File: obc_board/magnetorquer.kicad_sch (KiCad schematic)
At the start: 44 parts

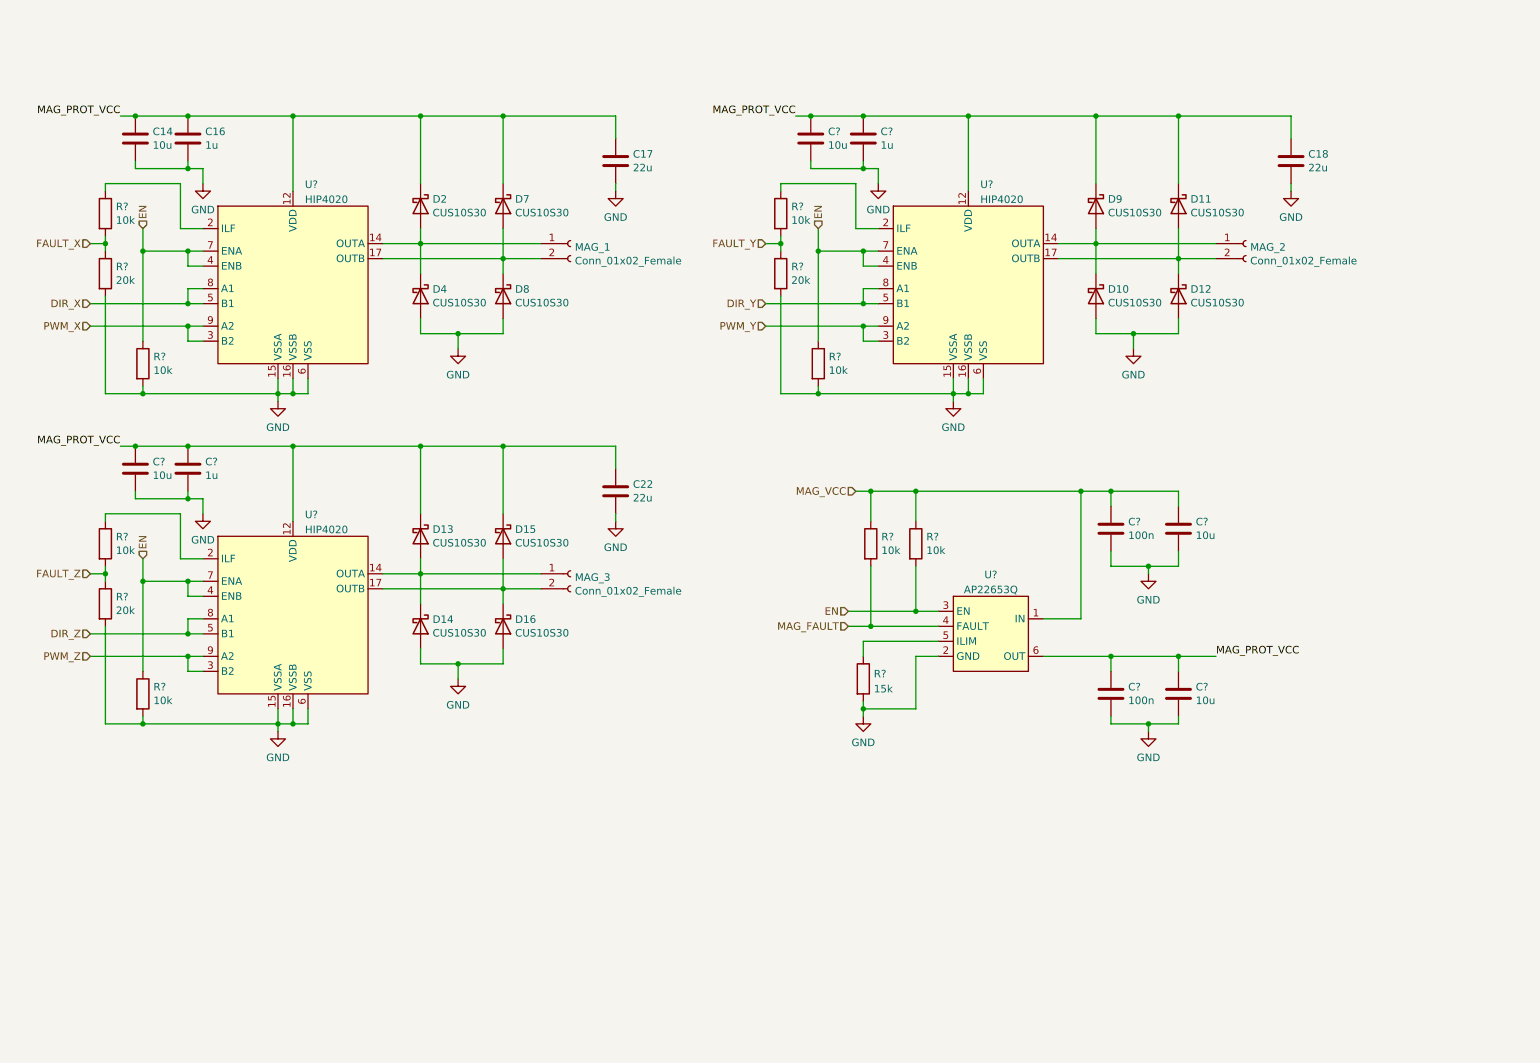
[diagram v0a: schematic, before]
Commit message: changed magnetorquer driver IC and changed power switch IC
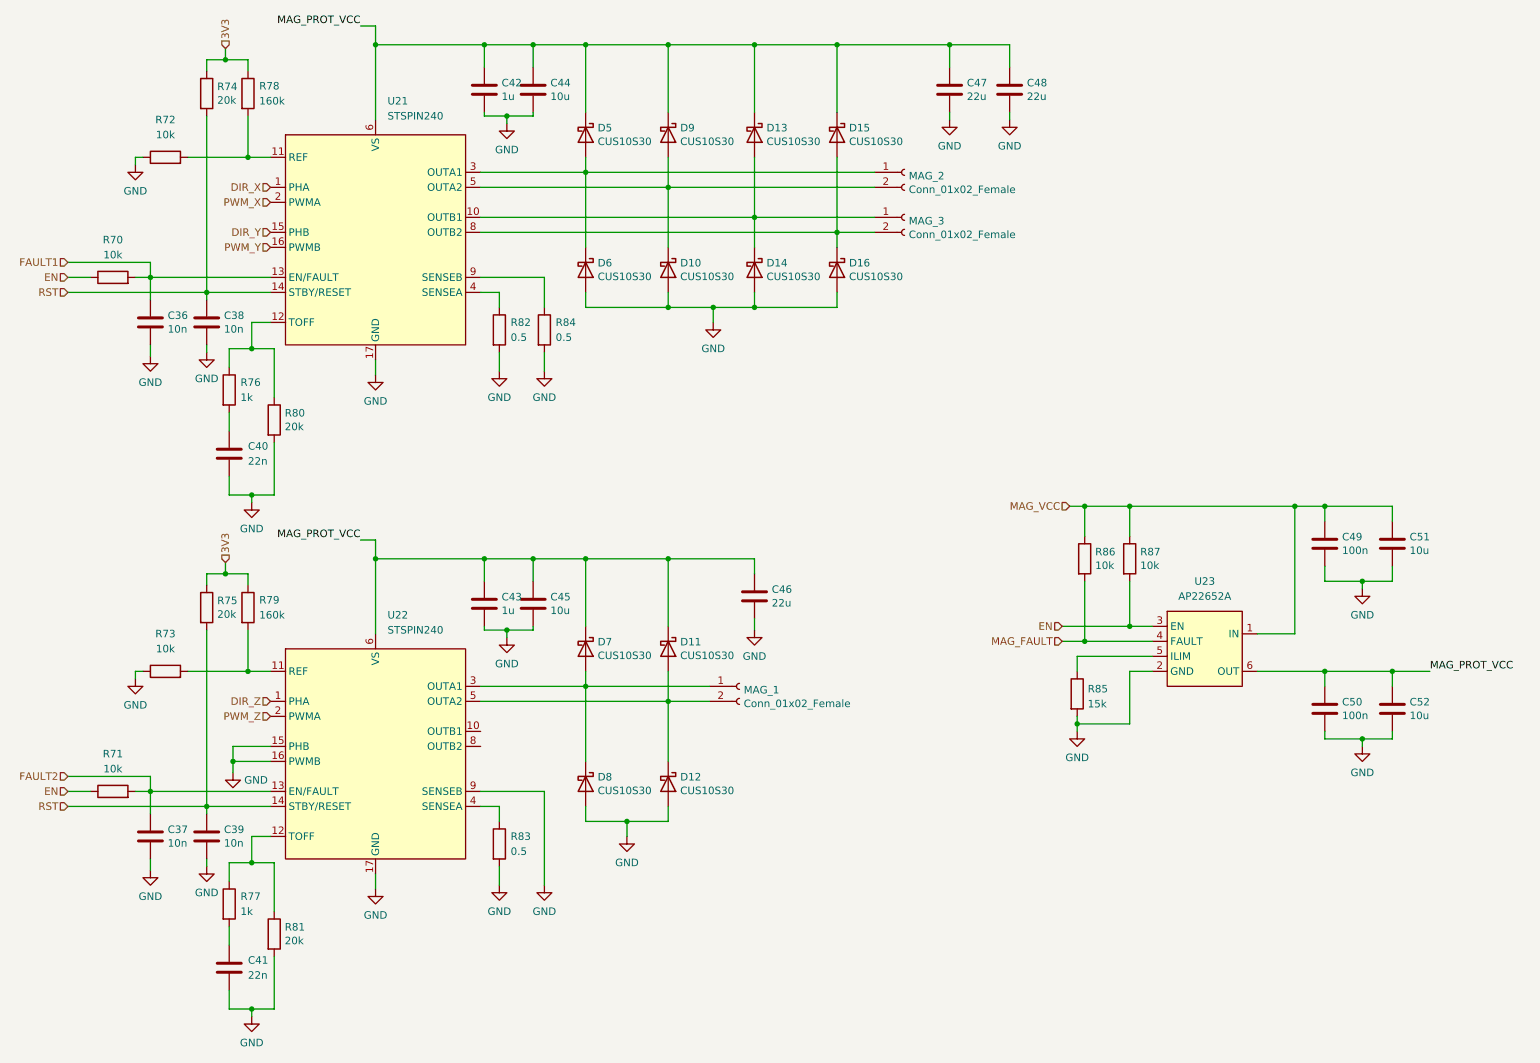
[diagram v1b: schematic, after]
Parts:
- removed C14, C? (x2): 10u, Capacitor_SMD:C_1206_3216Metric, symbol Device:C
- removed C16, C? (x2): 1u, Capacitor_SMD:C_0603_1608Metric, symbol Device:C
- removed R? (x6): 10k, Resistor_SMD:R_0402_1005Metric, symbol Device:R
- removed R? (x3): 20k, Resistor_SMD:R_0603_1608Metric, symbol Device:R
- removed U? (x3): HIP4020, symbol cubesat_obc_lib:HIP4020
- removed U?: AP22653Q, symbol cubesat_obc_lib:AP22653Q
- added C36, C37, C38, C39: 10n, Capacitor_SMD:C_0805_2012Metric, symbol Device:C
- added C40, C41: 22n, symbol Device:C
- added C42, C43: 1u, Capacitor_SMD:C_0603_1608Metric, symbol Device:C
- added C44, C45: 10u, Capacitor_SMD:C_1206_3216Metric, symbol Device:C
- added R70, R71, R72, R73: 10k, Resistor_SMD:R_0402_1005Metric, symbol Device:R
- added R74, R75, R80, R81: 20k, Resistor_SMD:R_0603_1608Metric, symbol Device:R
- added R76, R77: 1k, Resistor_SMD:R_0402_1005Metric, symbol Device:R
- added R78, R79: 160k, symbol Device:R
- added R82, R83, R84: 0.5, symbol Device:R
- added U21, U22: STSPIN240, symbol cubesat_obc_lib:STSPIN240
- added U23: AP22652A, symbol cubesat_obc_lib:AP22652A
- gave numbers to parts that had none: 7
- renumbered C22 to C46, C18 to C47, C17 to C48, D8 to D10, D15 to D11, D16 to D12, D9 to D13, D10 to D14, D11 to D15, D12 to D16, D2 to D5, D4 to D6, D13 to D7, D14 to D8, D7 to D9, MAG_3 to MAG_1, MAG_1 to MAG_2, MAG_2 to MAG_3
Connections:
- net DIR_X: now also U21.1 (PHA)
- net DIR_Y: now also U21.15 (PHB)
- net DIR_Z: now also U22.1 (PHA)
- net EN: now also R70.1, R71.1, U23.3 (EN)
- net GND: now also C36.1, C37.1, C38.1, C39.1, C40.2, C41.2, C42.2, C43.2, C44.2, C45.2, R72.1, R73.1, R80.2, R81.2, R82.2, R83.2, R84.2, U21.17 (GND), U21.7 (GND), U22.15 (PHB), U22.16 (PWMB), U22.17 (GND), U22.7 (GND), U22.9 (SENSEB), U23.2 (GND)
- net MAG_FAULT: now also U23.4 (FAULT)
- net MAG_VCC: now also U23.1 (IN)
- net PWM_X: now also U21.2 (PWMA)
- net PWM_Y: now also U21.16 (PWMB)
- net PWM_Z: now also U22.2 (PWMA)
- net at D5.2 (A), D6.1 (K), MAG_2.1 (Pin_1): now also U21.3 (OUTA1)
- net at D10.1 (K), D9.2 (A), MAG_2.2 (Pin_2): now also U21.5 (OUTA2)
- net at D13.2 (A), D14.1 (K), MAG_3.1 (Pin_1): now also U21.10 (OUTB1)
- net at D15.2 (A), D16.1 (K), MAG_3.2 (Pin_2): now also U21.8 (OUTB2)
- net at D7.2 (A), D8.1 (K), MAG_1.1 (Pin_1): now also U22.3 (OUTA1)
- net at D11.2 (A), D12.1 (K), MAG_1.2 (Pin_2): now also U22.5 (OUTA2)
- net at R85.1: now also U23.5 (ILIM)
- net VDD renamed MAG_PROT_VCC
- net MAG_PROT_VCC: now also C42.1, C43.1, C44.1, C45.1, U21.6 (VS), U22.6 (VS), U23.6 (OUT)
- new net: R72.2, R78.2, U21.11 (REF)
- new net: R73.2, R79.2, U22.11 (REF)
- new net: R77.1, R81.1, U22.12 (TOFF)
- new net: R83.1, U22.4 (SENSEA)
- new net: C41.1, R77.2
- new net: R76.1, R80.1, U21.12 (TOFF)
- new net: R82.1, U21.4 (SENSEA)
- new net: C40.1, R76.2
- new net: R84.1, U21.9 (SENSEB)
- new net 3V3: R74.1, R75.1, R78.1, R79.1
- new net FAULT1: C36.2, R70.2, U21.13 (EN/FAULT)
- new net FAULT2: C37.2, R71.2, U22.13 (EN/FAULT)
- new net RST: C38.2, C39.2, R74.2, R75.2, U21.14 (STBY/RESET), U22.14 (STBY/RESET)
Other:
- moved on the sheet: C46, C47, C48, C49, C50, C51, C52, D10, D11, D12, D13, D14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

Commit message: updated digikey part numbers and footprints
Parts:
- C36, C37, C38, C39: footprint Capacitor_SMD:C_0805_2012Metric -> Capacitor_SMD:C_0603_1608Metric; Digikey Part Number 490-8295-1-ND -> 399-14104-1-ND
- C40, C41: footprint (none) -> Capacitor_SMD:C_0402_1005Metric; Digikey Part Number (none) -> 399-16022-1-ND
- C42, C43: Digikey Part Number 311-1446-2-ND -> 399-17713-1-ND
- C44, C45, C51, C52: Digikey Part Number 311-1952-1-ND -> 399-7012-1-ND
- C46, C47, C48: footprint Capacitor_SMD:C_1206_3216Metric -> Capacitor_SMD:C_1210_3225Metric; Digikey Part Number 311-1995-1-ND -> 399-13723-1-ND
- C49, C50: Digikey Part Number 490-16433-1-ND -> 399-6828-1-ND
- MAG_1, MAG_2, MAG_3: Digikey Part Number WM7620CT-ND -> WM25389CT-ND
- R70, R71, R72, R73, R86, R87: Digikey Part Number 311-10.0KLRCT-ND -> YAG3436CT-ND
- R74, R75, R80, R81: Digikey Part Number 764-1399-1-ND -> YAG3577CT-ND
- R76, R77: Digikey Part Number 311-1.00KLRCT-ND -> 311-1KLBCT-ND
- R78, R79: footprint (none) -> Resistor_SMD:R_0402_1005Metric; Digikey Part Number (none) -> YAG5635CT-ND
- R82, R83, R84: footprint (none) -> Resistor_SMD:R_0805_2012Metric; Digikey Part Number (none) -> 311-.5LUCT-ND
- R85: footprint (none) -> Resistor_SMD:R_0402_1005Metric; Digikey Part Number (none) -> YAG3444CT-ND
- U21, U22: footprint (none) -> Package_DFN_QFN:VQFN-16-1EP_3x3mm_P0.5mm_EP1.68x1.68mm_ThermalVias; Digikey Part Number (none) -> 497-16604-1-ND
- U23: footprint (none) -> Package_TO_SOT_SMD:SOT-23-6; Digikey Part Number (none) -> 31-AP22652AW6-7CT-ND

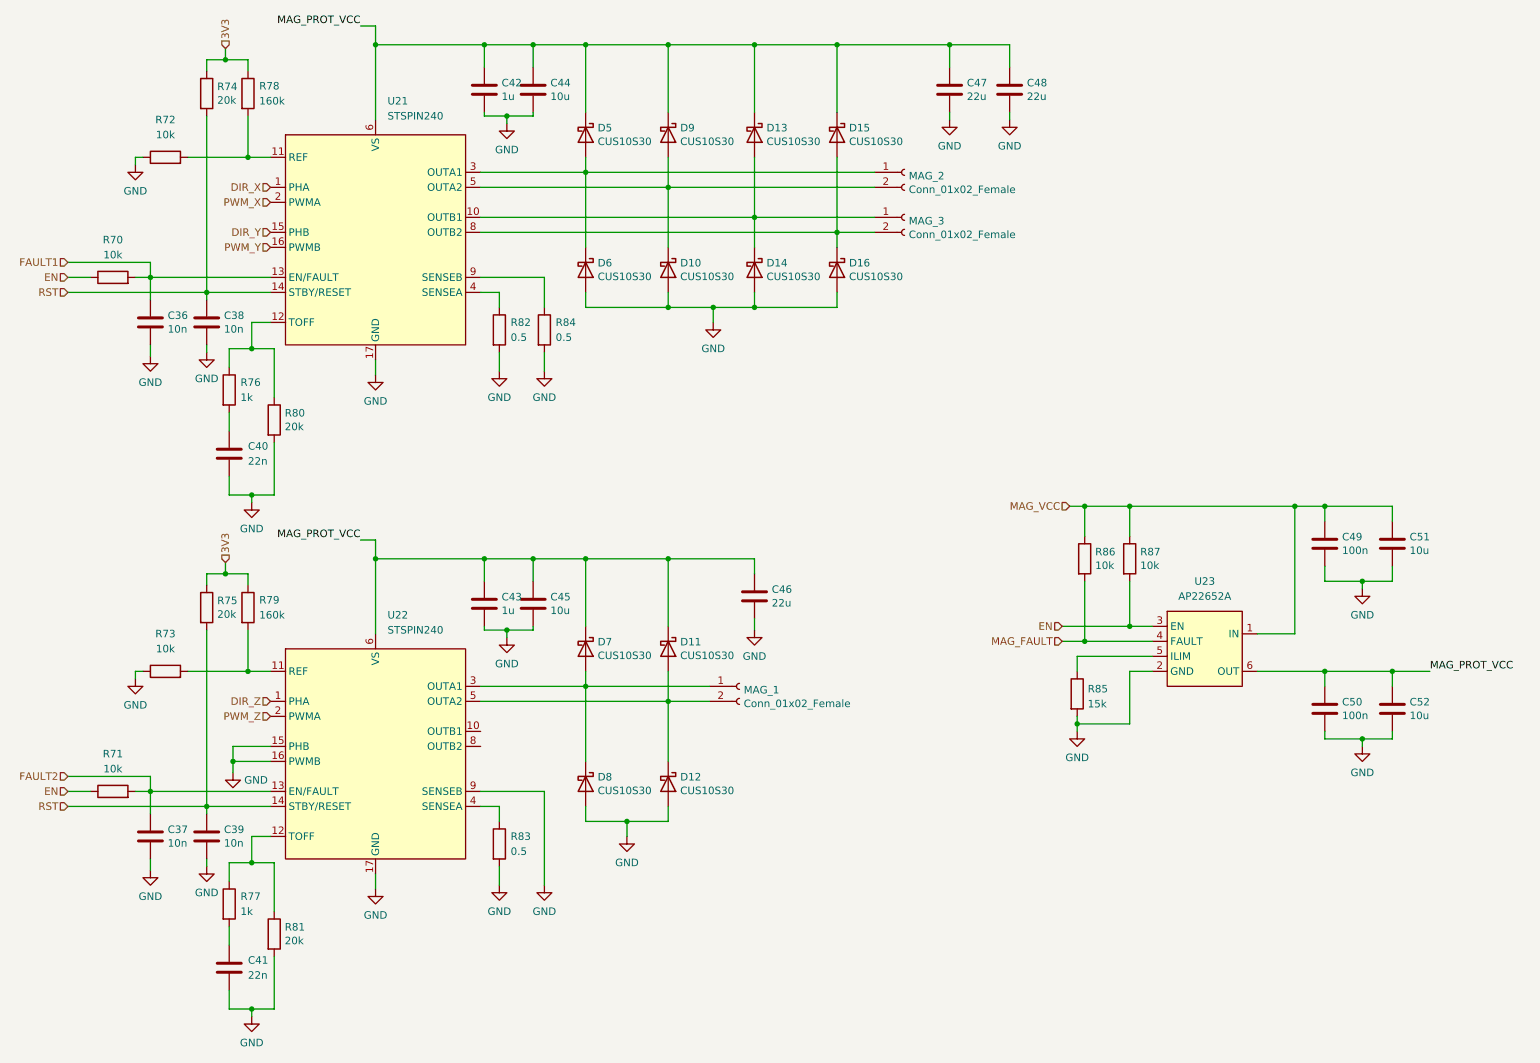
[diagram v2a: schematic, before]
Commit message: routed most of board
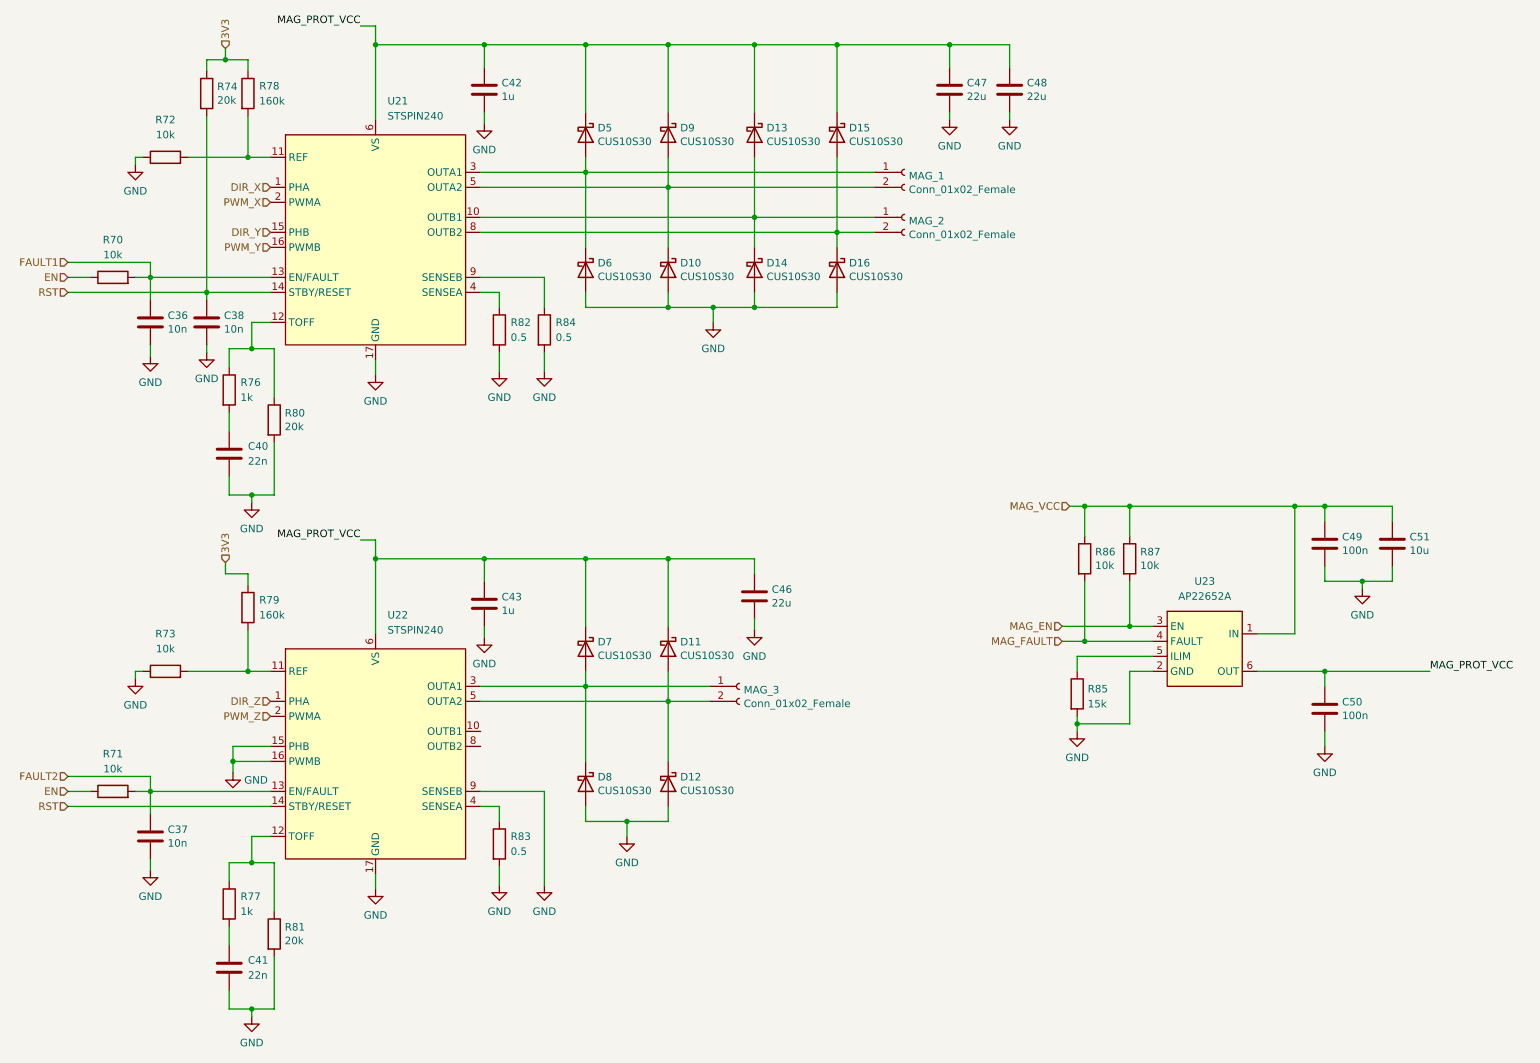
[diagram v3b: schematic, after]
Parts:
- removed C39: 10n, Capacitor_SMD:C_0603_1608Metric, symbol Device:C
- removed C44, C45, C52: 10u, Capacitor_SMD:C_1206_3216Metric, symbol Device:C
- removed R75: 20k, Resistor_SMD:R_0603_1608Metric, symbol Device:R
- renumbered MAG_3 to MAG_1, MAG_1 to MAG_2, MAG_2 to MAG_3
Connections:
- net EN: no longer R87.2, U23.3 (EN)
- net at D5.2 (A), D6.1 (K), U21.3 (OUTA1): now also MAG_1.1 (Pin_1); no longer MAG_3.1 (Pin_1)
- net at D10.1 (K), D9.2 (A), U21.5 (OUTA2): now also MAG_1.2 (Pin_2); no longer MAG_3.2 (Pin_2)
- net at D13.2 (A), D14.1 (K), U21.10 (OUTB1): now also MAG_2.1 (Pin_1); no longer MAG_1.1 (Pin_1)
- net at D15.2 (A), D16.1 (K), U21.8 (OUTB2): now also MAG_2.2 (Pin_2); no longer MAG_1.2 (Pin_2)
- net at D7.2 (A), D8.1 (K), U22.3 (OUTA1): now also MAG_3.1 (Pin_1); no longer MAG_2.1 (Pin_1)
- net at D11.2 (A), D12.1 (K), U22.5 (OUTA2): now also MAG_3.2 (Pin_2); no longer MAG_2.2 (Pin_2)
- new net MAG_EN: R87.2, U23.3 (EN)
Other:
- moved on the sheet: MAG_1, MAG_2, MAG_3

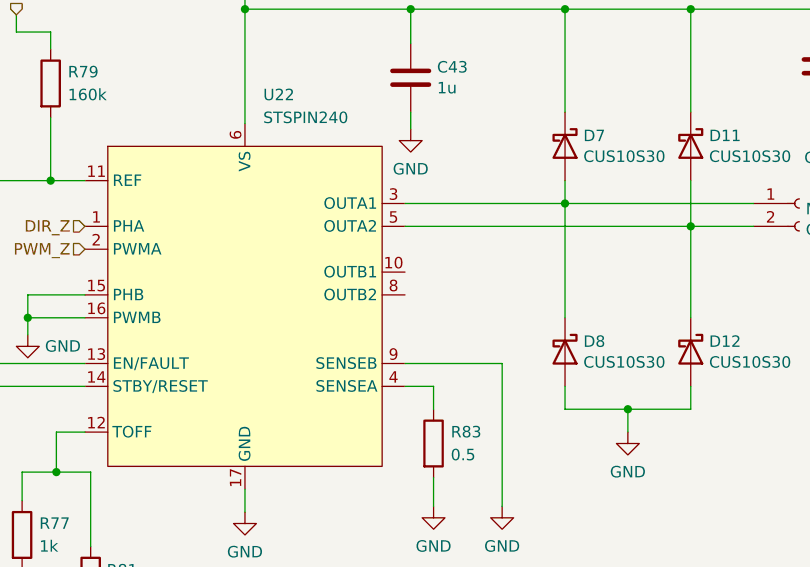
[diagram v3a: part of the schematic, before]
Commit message: added silkscreen labels and gerber file
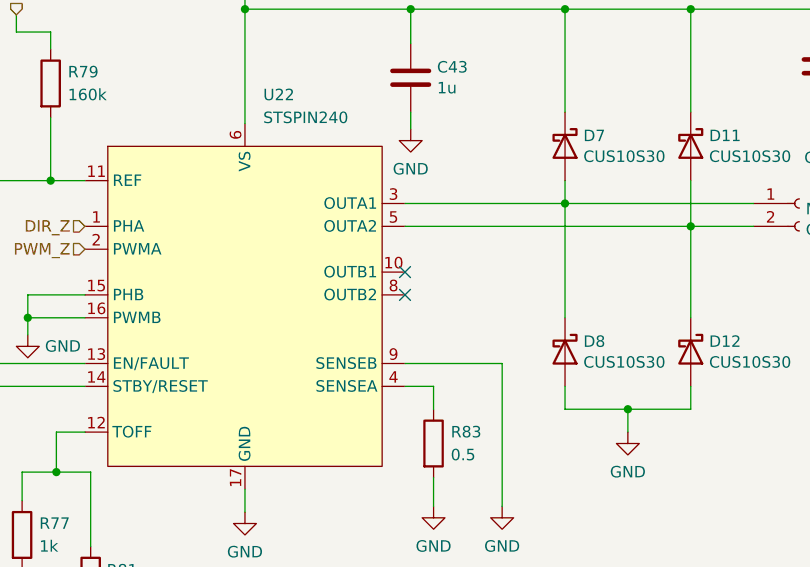
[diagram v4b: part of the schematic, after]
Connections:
- no-connect marks 0 -> 2
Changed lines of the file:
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@@
   (junction (at 119.38 109.22) (diameter 0) (color 0 0 0 0)
   )
+  (no_connect (at 101.6 140.97))
+  (no_connect (at 101.6 138.43))
   (wire (pts (xy 244.475 128.27) (xy 244.475 130.81))
     (stroke (width 0) (type default) (color 0 0 0 0))
